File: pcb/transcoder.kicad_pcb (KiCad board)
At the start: 2 copper layers, 74 x 41.8 mm, 35 parts, among them J1 MD-90SM, J2 Connector_RCA_2x3_REB, U1 BA7230LS, U2 LM1881, U3 THS7374

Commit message: Update
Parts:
- moved R13 45.6 mm to (175.2, 111.0), turned to 180 degrees
- moved R10 44.2 mm to (175.0, 106.0)
- moved R9 41.6 mm to (161.0, 111.0)
- moved R8 34.6 mm to (161.0, 101.0)
- moved C4 33.6 mm to (128.0, 83.0)
- moved R4 31.1 mm to (124.0, 83.0)
- moved C3 30.6 mm to (137.0, 83.0)
- moved R12 30.1 mm to (175.0, 92.0)
- moved R6 26.7 mm to (159.0, 87.2), turned to 90 degrees
- moved R3 25.9 mm to (133.0, 83.0)
- moved C14 25.0 mm to (161.0, 106.0), turned to 180 degrees
- moved U3 24.6 mm to (168.0, 93.0)
- moved C9 22.7 mm to (154.0, 113.0), turned to 0 degrees
- moved R7 20.6 mm to (163.0, 84.0)
- moved U2 20.5 mm to (146.8, 82.0)
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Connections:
- C1 pad 2: /R_IN -> /R
- C2 pad 2: /G_IN -> /G
- C3 pad 2: /B_IN -> /B
- C4 pad 2: /CVID_IN -> /CVID
- J2 pad 1: /Y_OUT -> /PR_OUT
- J2 pad 2: /PB_OUT -> unconnected-(J2-Composite-Pad2)
- J2 pad 3: /PR_OUT -> /PB_OUT
- J2 pad 4: /LAUD -> /RAUD
- J2 pad 5: /RAUD -> /Y_OUT
- J2 pad 6: unconnected-(J2-C-Pad6) -> /LAUD
- U1 pad 13: /R_IN -> /R
- U1 pad 14: /G_IN -> /G
- U1 pad 15: /B_IN -> /B
- U2 pad 2: /CVID_IN -> /CVID
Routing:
- net +5V: track 0.00 -> 129.1 mm, vias 0 -> 3
- net /LAUD: track 0.00 -> 69.7 mm
- net /CSYNC: track 0.00 -> 60.3 mm
- net /RAUD: track 0.00 -> 55.5 mm
- net /PB: track 0.00 -> 34.4 mm
- net /G: track 0.00 -> 33.9 mm, vias 0 -> 1
- net /B: track 0.00 -> 29.2 mm, vias 0 -> 1
- net /Y: track 0.00 -> 23.1 mm
- net /B_IN: track 0.00 -> 21.3 mm, vias 0 -> 1
- net Net-(U3-CH3_IN): track 0.00 -> 20.7 mm
- net Net-(U3-CH1_OUT): track 0.00 -> 20.5 mm
- net /CVID_IN: track 0.00 -> 20.1 mm
- net /PR: track 0.00 -> 19.6 mm
- net /CVID: track 0.00 -> 17.5 mm
- net Net-(U3-CH2_OUT): track 0.00 -> 15.4 mm
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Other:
- board size 74 x 41.8 mm -> 75.8 x 44 mm

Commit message: Minor tweaks
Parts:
- R5: value 680k -> 680K
- R6, R7: value 1k -> 1K
- R8, R9: value 2M2 -> 2.2M
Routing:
- net GND: vias 47 -> 56
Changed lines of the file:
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@@
         (effects (font (size 1 1) (thickness 0.15)))
     )
-    (fp_text value "2M2" (at 3.6 0) (layer "F.SilkS")
+    (fp_text value "2.2M" (at 3.6 0) (layer "F.SilkS")
         (effects (font (size 1 1) (thickness 0.15)))
     )
@@
         (effects (font (size 1 1) (thickness 0.15)))
     )
-    (fp_text value "680k" (at 0 2.2) (layer "F.SilkS")
+    (fp_text value "680K" (at 0 2.2) (layer "F.SilkS")
         (effects (font (size 1 1) (thickness 0.15)))
     )
@@
         (effects (font (size 1 1) (thickness 0.15)))
     )
-    (fp_text value "2M2" (at 3.8 0) (layer "F.SilkS")
+    (fp_text value "2.2M" (at 3.8 0) (layer "F.SilkS")
         (effects (font (size 1 1) (thickness 0.15)))
     )
@@
         (effects (font (size 1 1) (thickness 0.15)))
     )
-    (fp_text value "1k" (at 3 0 90) (layer "F.SilkS")
+    (fp_text value "1K" (at 3 0 90) (layer "F.SilkS")
         (effects (font (size 1 1) (thickness 0.15)))
     )
@@
         (effects (font (size 1 1) (thickness 0.15)))
     )
+    (fp_text user "Y" (at 10.2 -1.9 -90 unlocked) (layer "F.SilkS")
+        (effects (font (size 1 1) (thickness 0.15)) (justify bottom))
+    )
+    (fp_text user "Pb" (at -3.8 -1.9 -90 unlocked) (layer "F.SilkS")
+        (effects (font (size 1 1) (thickness 0.15)) (justify bottom))
+    )
+    (fp_text user "Pr" (at -13.75 -8 -90 unlocked) (layer "F.SilkS")
+        (effects (font (size 1.5 1.5) (thickness 0.15)) (justify bottom))
+    )
+    (fp_text user "CVid" (at -10.2 -1.9 -90 unlocked) (layer "F.SilkS")
+        (effects (font (size 1 1) (thickness 0.15)) (justify bottom))
+    )
+    (fp_text user "Y" (at 14.25 -7.75 -90 unlocked) (layer "F.SilkS")
+        (effects (font (size 1.5 1.5) (thickness 0.15)) (justify bottom))
+    )
+    (fp_text user "Left" (at 17.1 -1.9 -90 unlocked) (layer "F.SilkS")
+        (effects (font (size 1 1) (thickness 0.15)) (justify bottom))
+    )
+    (fp_text user "Pr" (at -17.2 -1.8 -90 unlocked) (layer "F.SilkS")
+        (effects (font (size 1 1) (thickness 0.15)) (justify bottom))
+    )
     (fp_text user "Right" (at 3.7 -1.9 -90 unlocked) (layer "F.SilkS")
         (effects (font (size 1 1) (thickness 0.15)) (justify bottom))
-    )
-    (fp_text user "Pb" (at -3.8 -1.9 -90 unlocked) (layer "F.SilkS")
-        (effects (font (size 1 1) (thickness 0.15)) (justify bottom))
-    )
-    (fp_text user "Left" (at 17.1 -1.9 -90 unlocked) (layer "F.SilkS")
-        (effects (font (size 1 1) (thickness 0.15)) (justify bottom))
-    )
-    (fp_text user "Pr" (at -13.75 -8 -90 unlocked) (layer "F.SilkS")
-        (effects (font (size 1.5 1.5) (thickness 0.15)) (justify bottom))
-    )
-    (fp_text user "CVid" (at -10.2 -1.9 -90 unlocked) (layer "F.SilkS")
-        (effects (font (size 1 1) (thickness 0.15)) (justify bottom))
-    )
-    (fp_text user "Y" (at 10.2 -1.9 -90 unlocked) (layer "F.SilkS")
-        (effects (font (size 1 1) (thickness 0.15)) (justify bottom))
-    )
-    (fp_text user "Pr" (at -17.2 -1.8 -90 unlocked) (layer "F.SilkS")
-        (effects (font (size 1 1) (thickness 0.15)) (justify bottom))
-    )
-    (fp_text user "Y" (at 14.25 -7.75 -90 unlocked) (layer "F.SilkS")
-        (effects (font (size 1.5 1.5) (thickness 0.15)) (justify bottom))
     )
     (fp_text user "Pb" (at 0.25 -7.75 -90 unlocked) (layer "F.SilkS")
@@
     (pad "9" thru_hole oval (at -17.6 -7.4 270) (size 2 3) (drill oval 1 2) (layers "*.Cu" "*.Mask")
       (net 6 "GND") (pinfunction "GND") (pintype "passive"))
-    (model "${KIPRJMOD}/Libraries/Models/CUI_DEVICES_RCJ-61_Series.step"
-      (offset (xyz 3.5 2.5 12.5))
-      (scale (xyz 1 1 1))
-      (rotate (xyz 0 -90 -90))
-    )
   )
   (footprint "REB_Transcoder:CUI_MD-90SM" (layer "F.Cu")
@@
         (effects (font (size 1 1) (thickness 0.15)))
     )
-    (fp_text value "1k" (at 3.2 0) (layer "F.SilkS")
+    (fp_text value "1K" (at 3.2 0) (layer "F.SilkS")
         (effects (font (size 1 1) (thickness 0.15)))
     )
@@
   (via (at 178.4 113.8) (size 0.6) (drill 0.3) (layers "F.Cu" "B.Cu") (free) (net 6))
   (via (at 170.8 113.8) (size 0.6) (drill 0.3) (layers "F.Cu" "B.Cu") (free) (net 6))
-  (via (at 141.04 76) (size 0.6) (drill 0.3) (layers "F.Cu" "B.Cu") (free) (net 6))
+  (via (at 141.4 76) (size 0.6) (drill 0.3) (layers "F.Cu" "B.Cu") (free) (net 6))
   (via (at 186 95.2) (size 0.6) (drill 0.3) (layers "F.Cu" "B.Cu") (free) (net 6))
   (via (at 165.2 113.8) (size 0.6) (drill 0.3) (layers "F.Cu" "B.Cu") (free) (net 6))
   (via (at 121.6 114.4) (size 0.6) (drill 0.3) (layers "F.Cu" "B.Cu") (free) (net 6))
   (via (at 190.2 109.2) (size 0.6) (drill 0.3) (layers "F.Cu" "B.Cu") (free) (net 6))
-  (via (at 151.2 89) (size 0.6) (drill 0.3) (layers "F.Cu" "B.Cu") (free) (net 6))
+  (via (at 150.333332 89) (size 0.6) (drill 0.3) (layers "F.Cu" "B.Cu") (free) (net 6))
   (via (at 190.2 80) (size 0.6) (drill 0.3) (layers "F.Cu" "B.Cu") (free) (net 6))
   (via (at 121.6 100.2) (size 0.6) (drill 0.3) (layers "F.Cu" "B.Cu") (free) (net 6))
@@
   (via (at 133.4 107.4) (size 0.6) (drill 0.3) (layers "F.Cu" "B.Cu") (free) (net 6))
   (via (at 121.6 106.8) (size 0.6) (drill 0.3) (layers "F.Cu" "B.Cu") (free) (net 6))
+  (via (at 151.4 110.6) (size 0.6) (drill 0.3) (layers "F.Cu" "B.Cu") (free) (net 6))
   (via (at 178.4 88.2) (size 0.6) (drill 0.3) (layers "F.Cu" "B.Cu") (free) (net 6))
   (via (at 170.6 81.6) (size 0.6) (drill 0.3) (layers "F.Cu" "B.Cu") (free) (net 6))
@@
   (via (at 165.8 98) (size 0.6) (drill 0.3) (layers "F.Cu" "B.Cu") (free) (net 6))
   (via (at 178.4 76) (size 0.6) (drill 0.3) (layers "F.Cu" "B.Cu") (free) (net 6))
-  (via (at 146.3 89) (size 0.6) (drill 0.3) (layers "F.Cu" "B.Cu") (free) (net 6))
+  (via (at 142.4 116.6) (size 0.6) (drill 0.3) (layers "F.Cu" "B.Cu") (free) (net 6))
+  (via (at 145.866666 89) (size 0.6) (drill 0.3) (layers "F.Cu" "B.Cu") (free) (net 6))
   (via (at 190.2 86.8) (size 0.6) (drill 0.3) (layers "F.Cu" "B.Cu") (free) (net 6))
   (via (at 186 109.2) (size 0.6) (drill 0.3) (layers "F.Cu" "B.Cu") (free) (net 6))
   (via (at 186 81.4) (size 0.6) (drill 0.3) (layers "F.Cu" "B.Cu") (free) (net 6))
+  (via (at 161.4 116.4) (size 0.6) (drill 0.3) (layers "F.Cu" "B.Cu") (free) (net 6))
   (via (at 131.8 76) (size 0.6) (drill 0.3) (layers "F.Cu" "B.Cu") (free) (net 6))
   (via (at 160.8 104.2) (size 0.6) (drill 0.3) (layers "F.Cu" "B.Cu") (free) (net 6))
   (via (at 121.8 78) (size 0.6) (drill 0.3) (layers "F.Cu" "B.Cu") (free) (net 6))
   (via (at 137.8 107.4) (size 0.6) (drill 0.3) (layers "F.Cu" "B.Cu") (free) (net 6))
+  (via (at 141.4 83.4) (size 0.6) (drill 0.3) (layers "F.Cu" "B.Cu") (free) (net 6))
   (via (at 173.2 95.2) (size 0.6) (drill 0.3) (layers "F.Cu" "B.Cu") (free) (net 6))
   (via (at 157.8 110.6) (size 0.6) (drill 0.3) (layers "F.Cu" "B.Cu") (free) (net 6))
   (via (at 154.8 89) (size 0.6) (drill 0.3) (layers "F.Cu" "B.Cu") (free) (net 6))
   (via (at 121.6 87.4) (size 0.6) (drill 0.3) (layers "F.Cu" "B.Cu") (free) (net 6))
+  (via (at 170.6 87) (size 0.6) (drill 0.3) (layers "F.Cu" "B.Cu") (free) (net 6))
+  (via (at 164.4 80) (size 0.6) (drill 0.3) (layers "F.Cu" "B.Cu") (free) (net 6))
+  (via (at 157.6 80) (size 0.6) (drill 0.3) (layers "F.Cu" "B.Cu") (free) (net 6))
   (via (at 169.2 99.6) (size 0.6) (drill 0.3) (layers "F.Cu" "B.Cu") (free) (net 6))
   (via (at 190.2 100) (size 0.6) (drill 0.3) (layers "F.Cu" "B.Cu") (free) (net 6))
@@
   (via (at 171.6 103) (size 0.6) (drill 0.3) (layers "F.Cu" "B.Cu") (free) (net 6))
   (via (at 121.6 93.4) (size 0.6) (drill 0.3) (layers "F.Cu" "B.Cu") (free) (net 6))
+  (via (at 175.2 116.6) (size 0.6) (drill 0.3) (layers "F.Cu" "B.Cu") (free) (net 6))
   (via (at 186 103.5) (size 0.6) (drill 0.3) (layers "F.Cu" "B.Cu") (free) (net 6))
   (via (at 140.8 111.4) (size 0.6) (drill 0.3) (layers "F.Cu" "B.Cu") (free) (net 6))
+  (via (at 159.6 93) (size 0.6) (drill 0.3) (layers "F.Cu" "B.Cu") (free) (net 6))
   (via (at 135.6 105) (size 0.6) (drill 0.3) (layers "F.Cu" "B.Cu") (free) (net 6))
   (via (at 155.8 102.2) (size 0.6) (drill 0.3) (layers "F.Cu" "B.Cu") (free) (net 6))

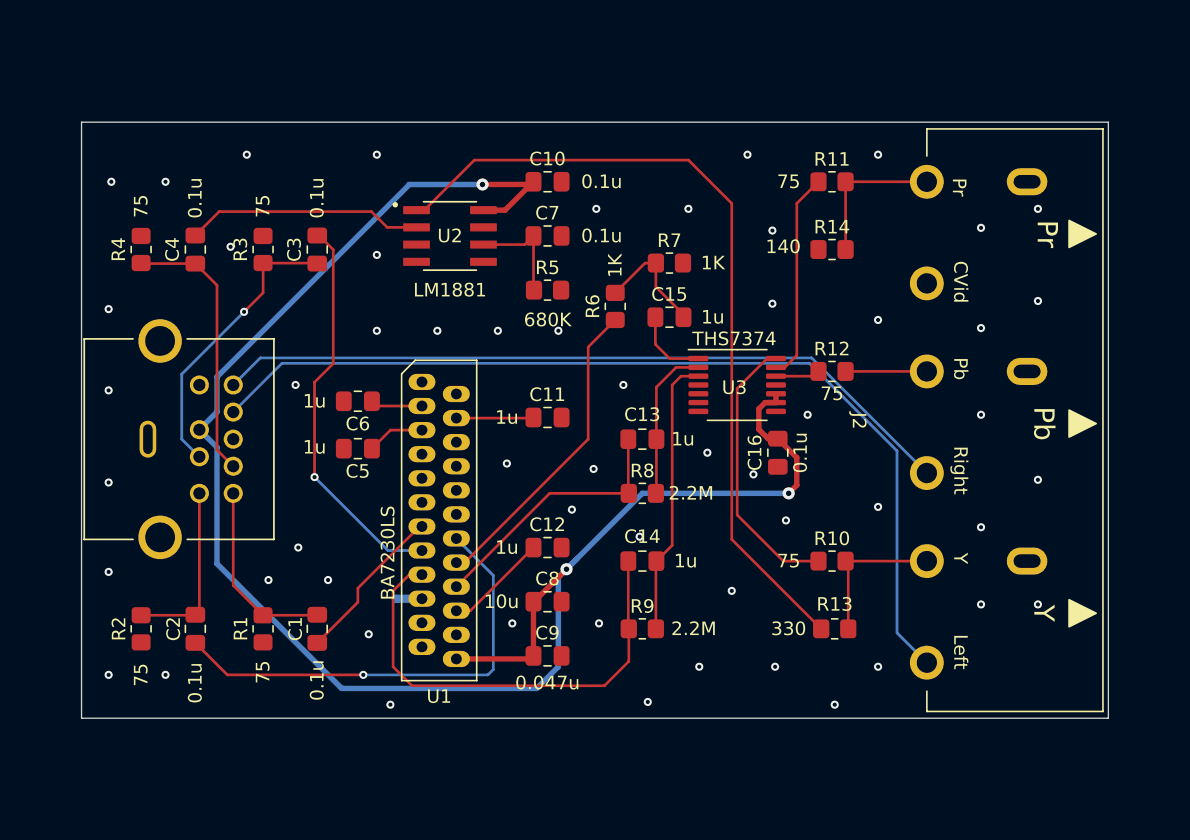
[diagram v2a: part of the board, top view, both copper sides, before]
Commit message: Mounting holes
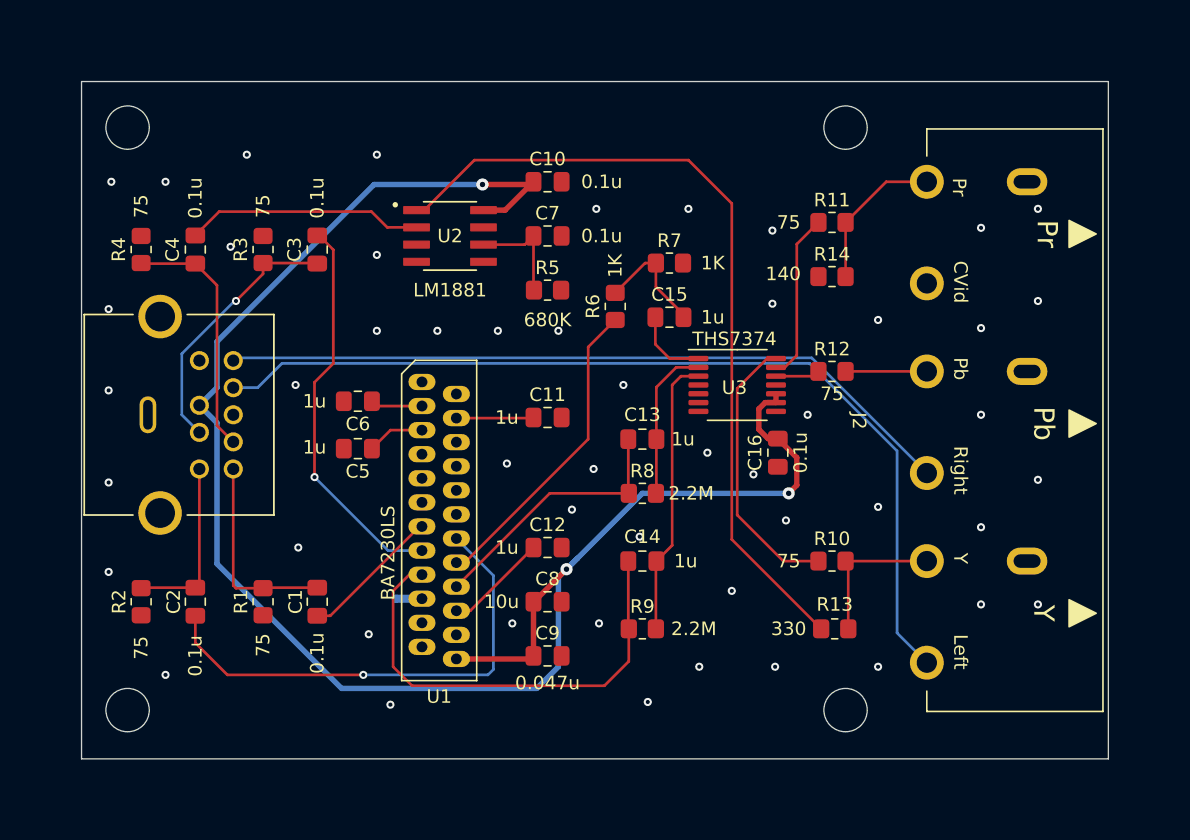
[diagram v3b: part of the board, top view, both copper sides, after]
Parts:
- added M0: MountingHole_3.2mm_M3, MountingHole:MountingHole_3.2mm_M3, F.Cu at (123.0, 117.0)
- added M0: MountingHole_3.2mm_M3, MountingHole:MountingHole_3.2mm_M3, F.Cu at (176.0, 117.0)
- added M0: MountingHole_3.2mm_M3, MountingHole:MountingHole_3.2mm_M3, F.Cu at (176.0, 74.0)
- added M0: MountingHole_3.2mm_M3, MountingHole:MountingHole_3.2mm_M3, F.Cu at (123.0, 74.0)
- moved R11 3.00 mm to (175.0, 81.0)
- moved C1 2.00 mm to (137.0, 109.0)
- moved C2 2.00 mm to (128.0, 109.0)
- moved R1 2.00 mm to (133.0, 109.0)
- moved R14 2.00 mm to (175.0, 85.0)
- moved R2 2.00 mm to (124.0, 109.0)
- moved J1 1.80 mm to (124.5, 95.2)
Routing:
- net Net-(U3-CH2_OUT): track 15.4 -> 12.4 mm
- net /G: track 33.9 -> 35.9 mm
- net /CVID_IN: track 20.1 -> 18.3 mm
- net /B_IN: track 21.3 -> 19.6 mm
- net +5V: track 129.1 -> 130.6 mm
- net /R: track 11.9 -> 10.5 mm
- net /R_IN: track 13.9 -> 14.9 mm
- net /LAUD: track 69.7 -> 69.0 mm
- net /RAUD: track 55.5 -> 54.8 mm
- net GND: vias 56 -> 50
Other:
- board size 75.8 x 44 mm -> 75.8 x 50 mm

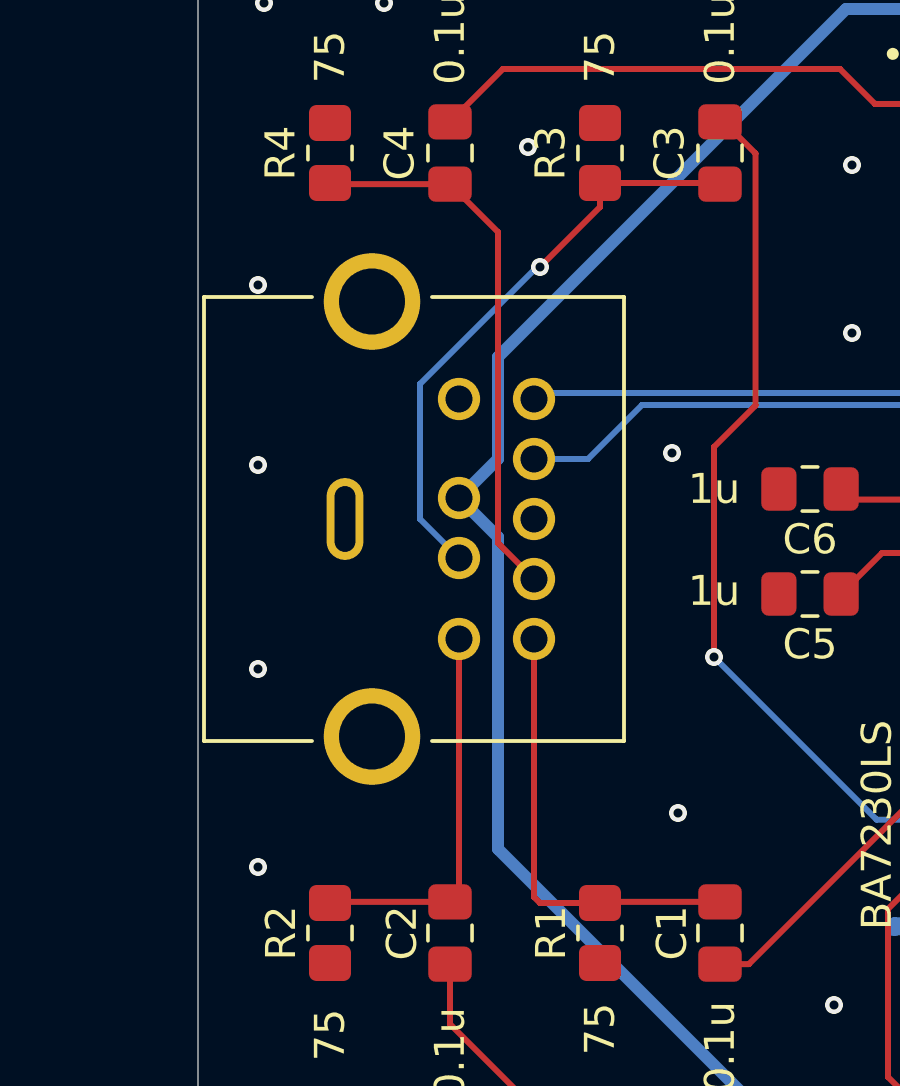
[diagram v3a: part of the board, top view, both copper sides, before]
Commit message: Fix ordering of filter/termination on inputs
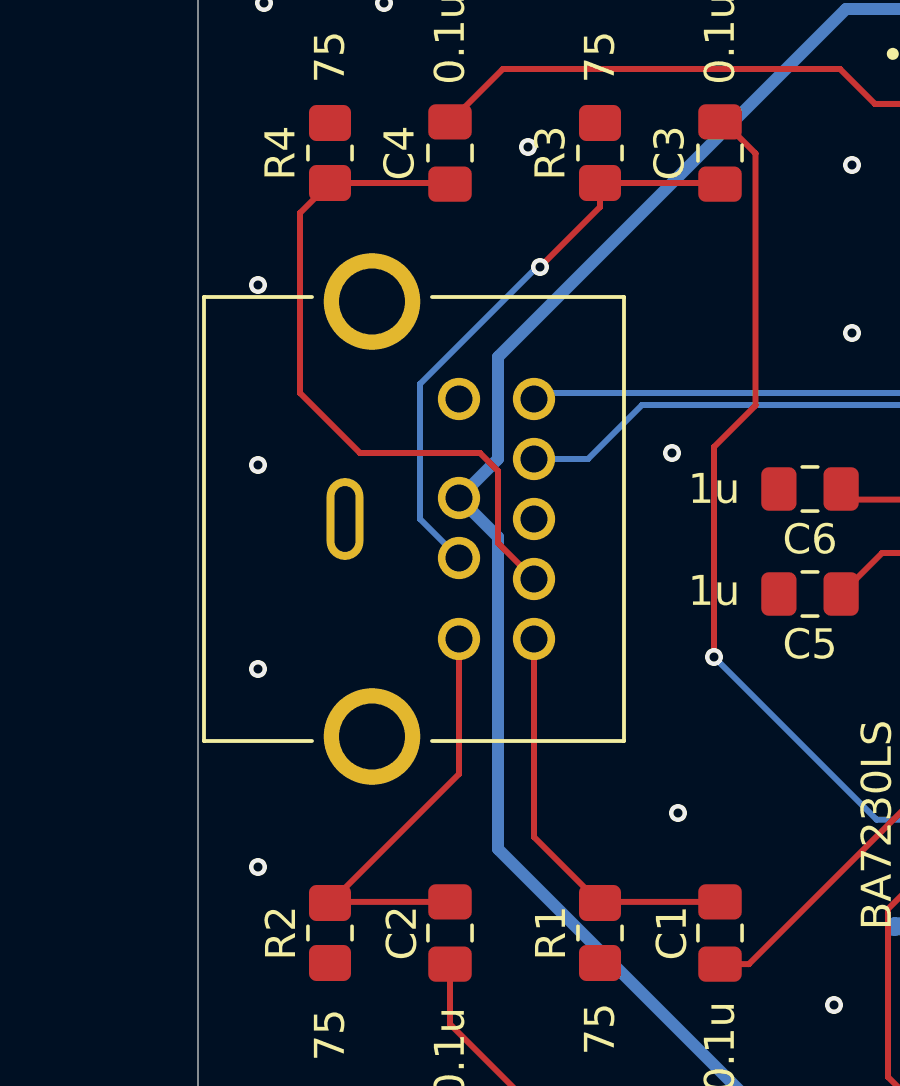
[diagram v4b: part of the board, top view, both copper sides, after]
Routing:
- net /CVID_IN: track 18.3 -> 23.2 mm
- net /G_IN: track 12.9 -> 14.6 mm
- net /R_IN: track 14.9 -> 13.7 mm
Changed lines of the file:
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@@
     (stroke (width 0.0381) (type default)) (fill none) (layer "Edge.Cuts"))
   (segment (start 133.0375 107.9625) (end 137 107.9625) (width 0.2) (layer "F.Cu") (net 1))
-  (segment (start 130.8 99.2) (end 130.8 107.8) (width 0.2) (layer "F.Cu") (net 1))
-  (segment (start 131 108) (end 133 108) (width 0.2) (layer "F.Cu") (net 1))
+  (segment (start 130.8 105.8) (end 133 108) (width 0.2) (layer "F.Cu") (net 1))
+  (segment (start 130.8 99.2) (end 130.8 105.8) (width 0.2) (layer "F.Cu") (net 1))
   (segment (start 133 108) (end 133.0375 107.9625) (width 0.2) (layer "F.Cu") (net 1))
-  (segment (start 130.8 107.8) (end 131 108) (width 0.2) (layer "F.Cu") (net 1))
   (segment (start 124 108) (end 124.0375 107.9625) (width 0.2) (layer "F.Cu") (net 2))
-  (segment (start 128.3 107.6625) (end 128 107.9625) (width 0.2) (layer "F.Cu") (net 2))
   (segment (start 124.0375 107.9625) (end 128 107.9625) (width 0.2) (layer "F.Cu") (net 2))
-  (segment (start 128.3 99.2) (end 128.3 107.6625) (width 0.2) (layer "F.Cu") (net 2))
+  (segment (start 128.3 103.7) (end 124 108) (width 0.2) (layer "F.Cu") (net 2))
+  (segment (start 128.3 99.2) (end 128.3 103.7) (width 0.2) (layer "F.Cu") (net 2))
   (segment (start 133 84) (end 136.9625 84) (width 0.2) (layer "F.Cu") (net 3))
   (segment (start 136.9625 84) (end 137 84.0375) (width 0.2) (layer "F.Cu") (net 3))
@@
   (segment (start 127 90.7) (end 127 95.2) (width 0.2) (layer "B.Cu") (net 3))
   (segment (start 127 95.2) (end 128.3 96.5) (width 0.2) (layer "B.Cu") (net 3))
+  (segment (start 129.6 93.6) (end 129.6 96) (width 0.2) (layer "F.Cu") (net 4))
+  (segment (start 125 93) (end 129 93) (width 0.2) (layer "F.Cu") (net 4))
+  (segment (start 123 91) (end 125 93) (width 0.2) (layer "F.Cu") (net 4))
+  (segment (start 124 84) (end 123 85) (width 0.2) (layer "F.Cu") (net 4))
   (segment (start 129.6 96) (end 130.8 97.2) (width 0.2) (layer "F.Cu") (net 4))
-  (segment (start 129.6 85.6375) (end 129.6 96) (width 0.2) (layer "F.Cu") (net 4))
-  (segment (start 124.0375 84.0375) (end 124 84) (width 0.2) (layer "F.Cu") (net 4))
-  (segment (start 128 84.0375) (end 124.0375 84.0375) (width 0.2) (layer "F.Cu") (net 4))
-  (segment (start 128 84.0375) (end 129.6 85.6375) (width 0.2) (layer "F.Cu") (net 4))
+  (segment (start 129 93) (end 129.6 93.6) (width 0.2) (layer "F.Cu") (net 4))
+  (segment (start 123 85) (end 123 91) (width 0.2) (layer "F.Cu") (net 4))
+  (segment (start 124 84) (end 127.9625 84) (width 0.2) (layer "F.Cu") (net 4))
+  (segment (start 127.9625 84) (end 128 84.0375) (width 0.2) (layer "F.Cu") (net 4))
   (segment (start 141.0375 97.7) (end 142.405 96.3325) (width 0.2) (layer "F.Cu") (net 5))
   (segment (start 142.405 96.3325) (end 144.73 96.3325) (width 0.2) (layer "F.Cu") (net 5))
